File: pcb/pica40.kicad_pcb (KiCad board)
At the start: 2 copper layers, 135 x 95.7 mm, 67 parts, among them SW1 SW_PUSH, SW10 SW_PUSH, SW11 SW_PUSH, SW12 SW_PUSH, SW13 SW_PUSH, SW14 SW_PUSH, SW15 SW_PUSH, SW16 SW_PUSH, SW17 SW_PUSH, SW18 SW_PUSH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

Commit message: update case files
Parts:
- moved BATTCONN1 11.8 mm to (196.8, 95.7), turned to -90 degrees
- moved USB1 9.00 mm to (203.6, 114.6)
- moved USB2 9.00 mm to (203.6, 114.6)
- moved H7 8.06 mm to (198.9, 106.2)
- moved LED1 6.74 mm to (193.3, 102.1)
- moved H6 1.71 mm to (186.8, 106.2)
- moved RESET1 1.70 mm to (200.9, 96.7)
- moved G*** 0.67 mm to (120.7, 117.2) (x2)
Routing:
- net row6: track 40.4 -> 49.4 mm
- net row5: track 40.1 -> 49.1 mm
- net row7: track 42.2 -> 51.2 mm
- net row4: track 38.2 -> 47.2 mm
- net ENCA: track 62.5 -> 70.7 mm
- net ENCB: track 58.4 -> 66.6 mm
- net LED: track 41.8 -> 49.7 mm
- net RESET: track 54.3 -> 47.7 mm
- net VCC: track 47.6 -> 53.7 mm
- net BATT: track 54.7 -> 50.9 mm
- net col3: track 160.8 -> 162.9 mm
- net col4: track 119.2 -> 121.2 mm
- net col2: track 180.1 -> 181.9 mm
- net col1: track 255.3 -> 256.5 mm
- net col0: track 349.5 -> 350.1 mm
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
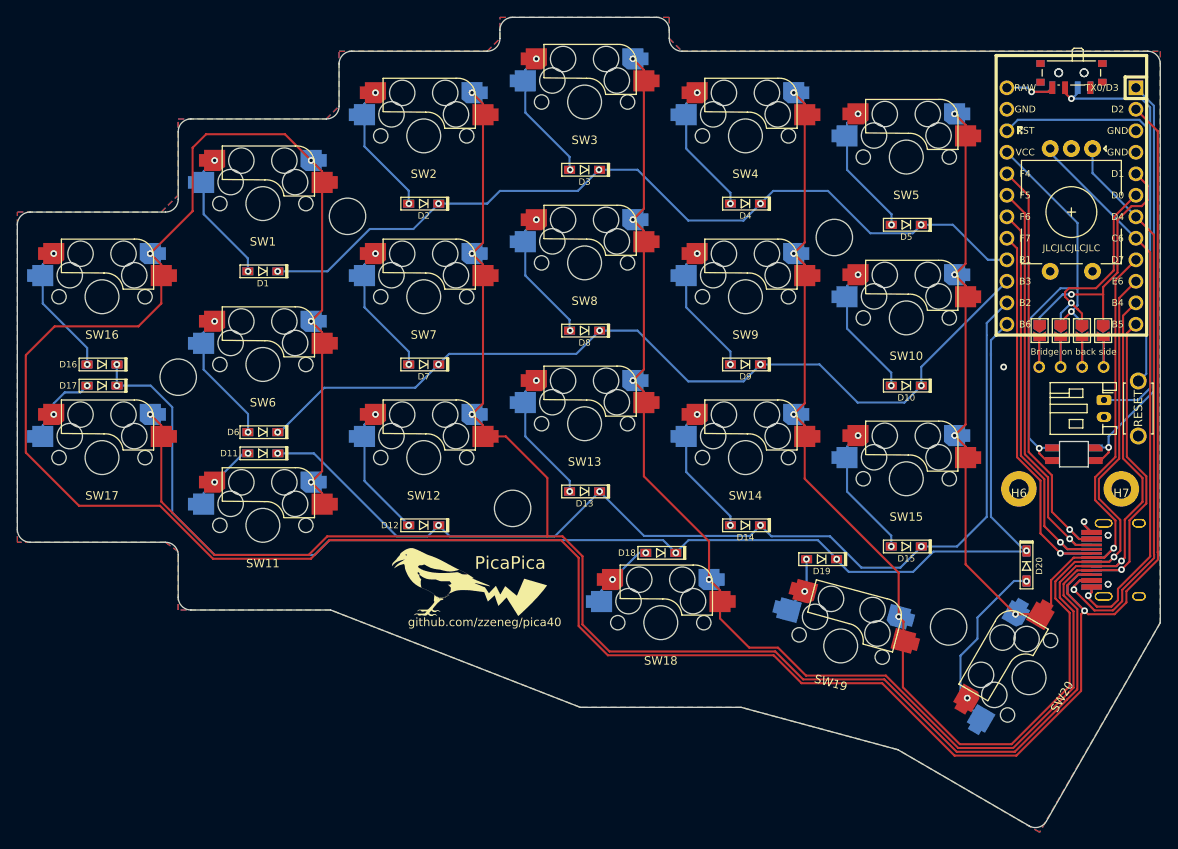
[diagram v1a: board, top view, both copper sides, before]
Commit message: use footprints with PTH slots
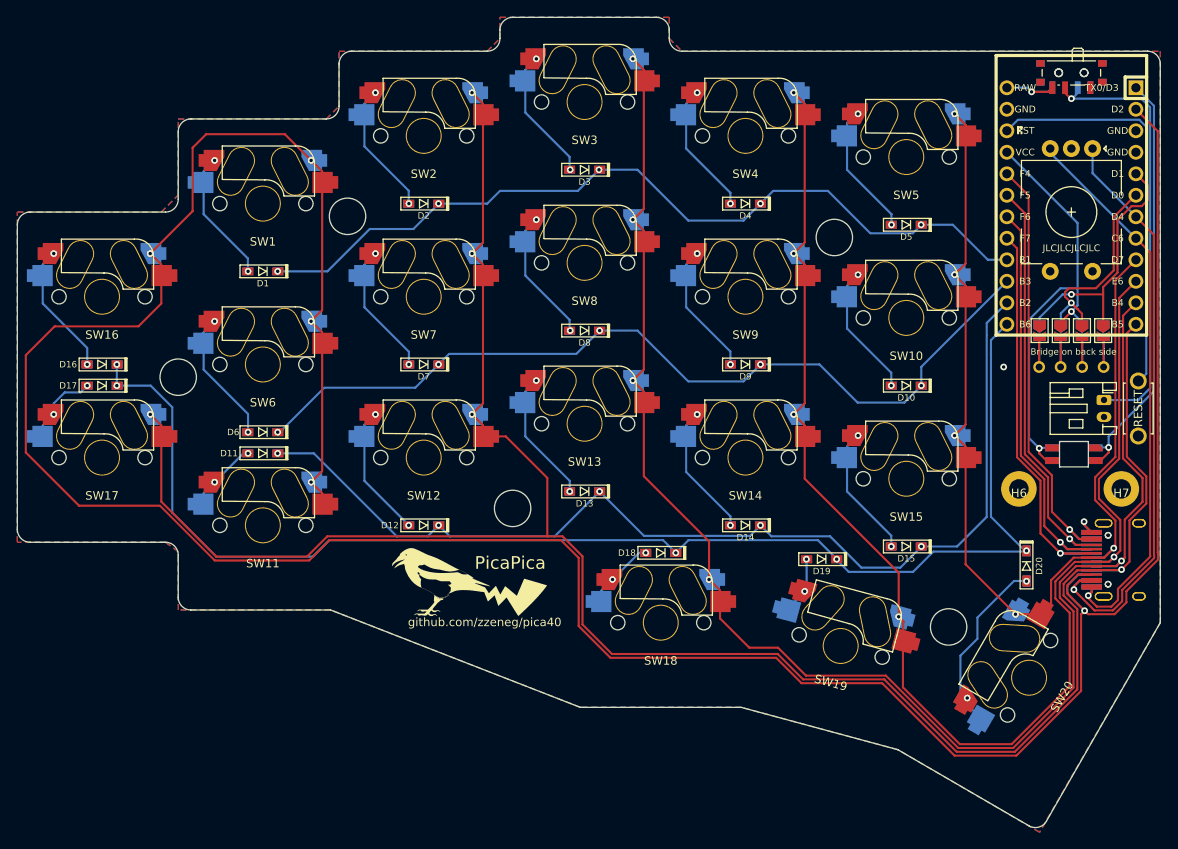
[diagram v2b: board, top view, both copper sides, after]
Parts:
- SW1, SW10, SW11, SW12, SW13, SW14, SW15, SW16, SW17, SW18, SW19, SW2, SW3, SW4, SW5, SW6, SW7, SW8, SW9: footprint pica:CherryMX_Hotswap -> pica:CherryMX_Hotswap_PTH
- SW20: footprint pica:CherryMX_Hotswap_1.5 -> pica:CherryMX_Hotswap_1.5_PTH

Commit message: Revert "use footprints with PTH slots"
This reverts commit bdcc6b4fc5c42f5b6ab726123ea9fec0ebe93fb2.
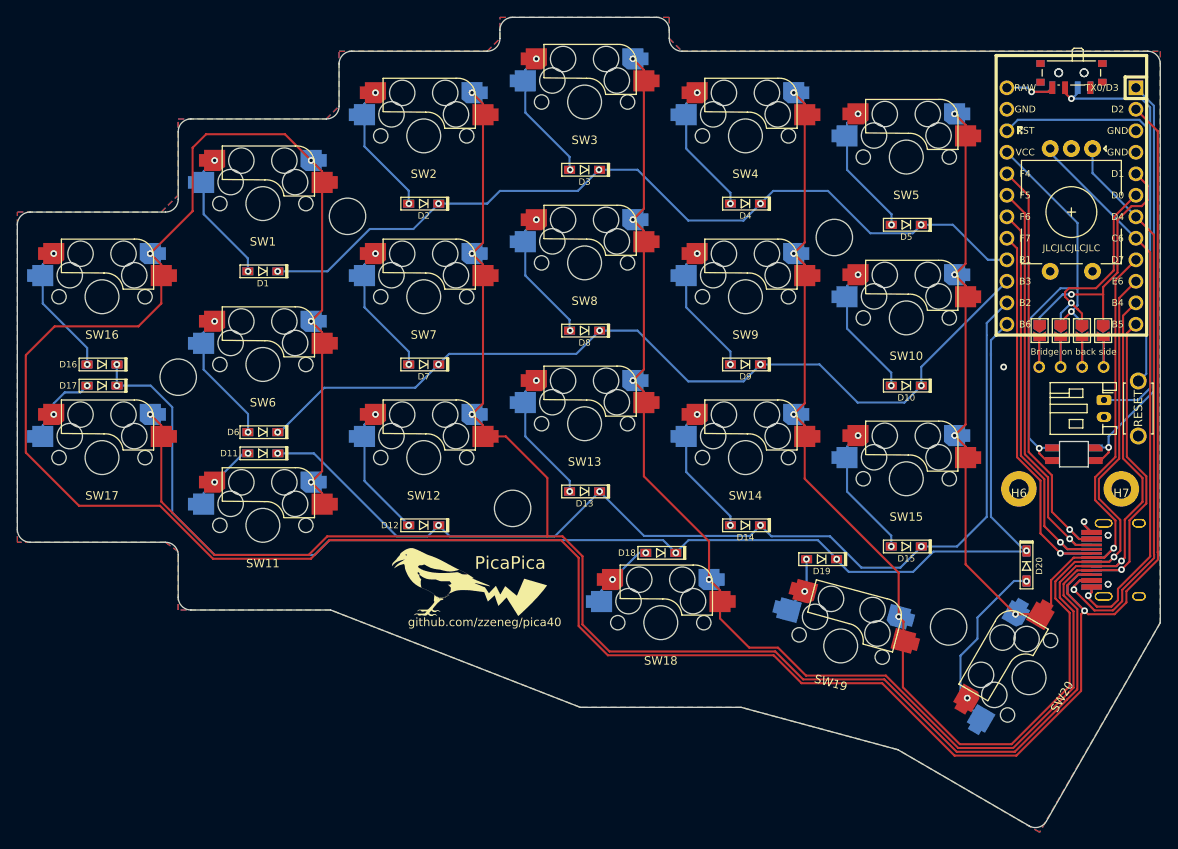
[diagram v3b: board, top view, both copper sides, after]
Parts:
- SW1, SW10, SW11, SW12, SW13, SW14, SW15, SW16, SW17, SW18, SW19, SW2, SW3, SW4, SW5, SW6, SW7, SW8, SW9: footprint pica:CherryMX_Hotswap_PTH -> pica:CherryMX_Hotswap
- SW20: footprint pica:CherryMX_Hotswap_1.5_PTH -> pica:CherryMX_Hotswap_1.5
